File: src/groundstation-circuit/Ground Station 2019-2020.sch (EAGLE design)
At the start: 9 parts, among them U1 ADAFRUIT_RFM95W_LORA_RADIO

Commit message: Schematic and first routing attempt completed.
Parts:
- removed D1, D2, D3: (no value), SparkFun-LED:LED5MM
- added LED1, LED2, LED3: (no value), SparkFun-LED:LED5MM
- added R4: 220, SparkFun-Resistors:330OHM-HORIZ-1/10W-5%
- added R5: 1000, SparkFun-Resistors:330OHM-HORIZ-1/10W-5%
- renumbered J1 to HC-05
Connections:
- new net 3.3V: HC-05.2, U$1.3.3V, U1.VIN
- new net CS: U$1.10/TX2/PWM, U1.CS
- new net G0: U$1.8/TX3, U1.G0
- new net LED1: R3.2, U$1.2
- new net LED2: R2.2, U$1.3/CAN-TX/PWM
- new net LED3: R1.2, U$1.4/CAN-RX-PWM
- new net MISO: U$1.12/MISO, U1.MISO
- new net MOSI: U$1.11/MOSI, U1.MOSI
- new net N$1: LED3.A, R1.1
- new net N$3: LED1.A, R3.1
- new net N$4: R4.2, U$1.1/TX1/T
- new net RST: U$1.9/RX2/PWM, U1.RST
- new net RX1: HC-05.4, U$1.0/RX1/T
- new net SCK: U$1.13/SCK/LED, U1.SCK
- new net TX1: HC-05.5, R4.1, R5.2
- net GND: now also HC-05.3, LED1.C, LED2.C, LED3.C, R5.1
- net N$2: now also LED2.A, R2.1; no longer U1.VIN
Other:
- moved on the sheet: R1, R2, R3

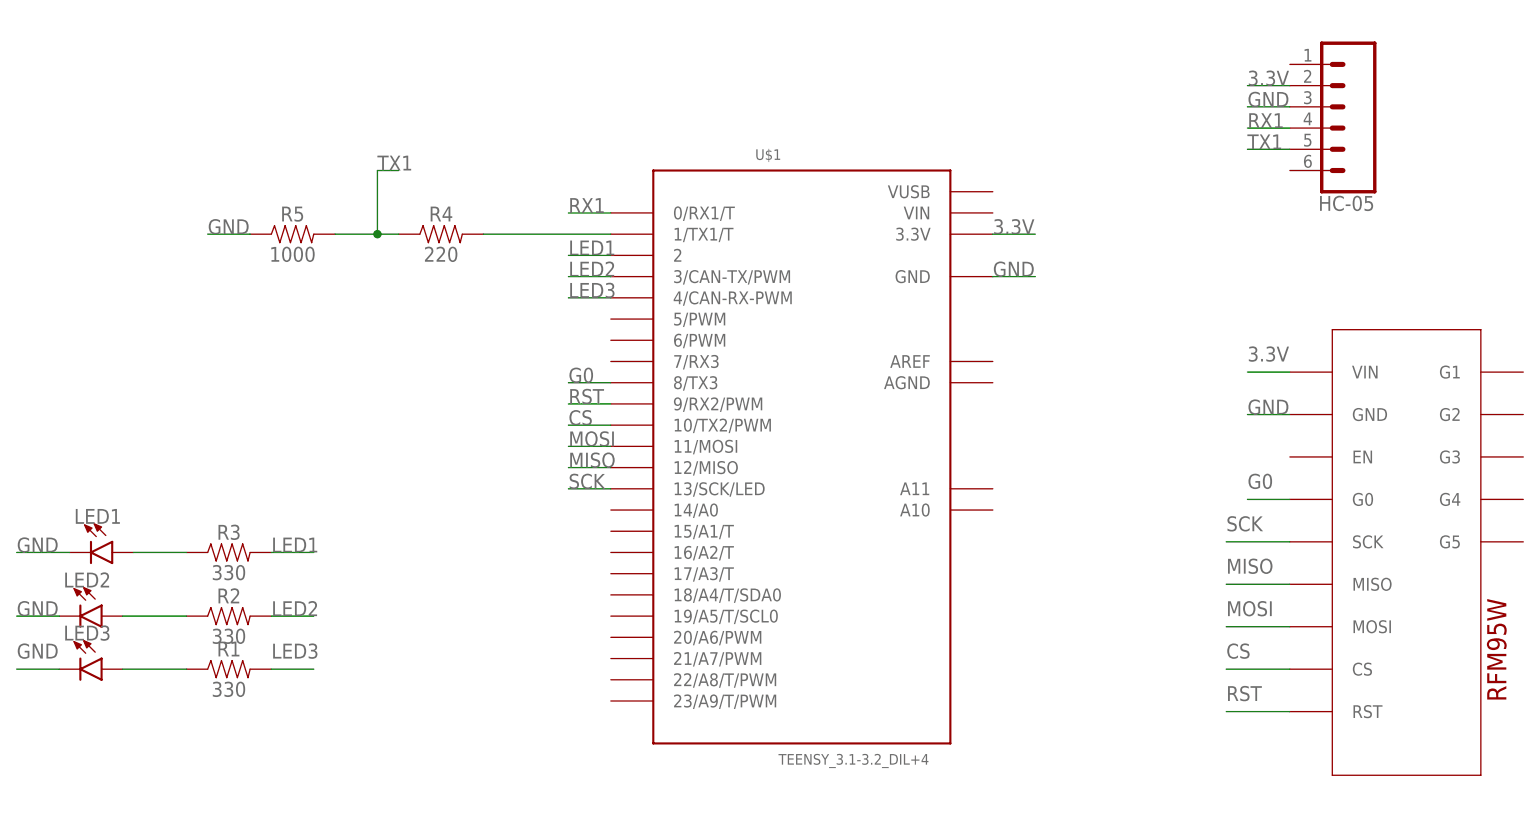
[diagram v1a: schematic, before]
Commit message: Added LCD to board and increased space to accomidate
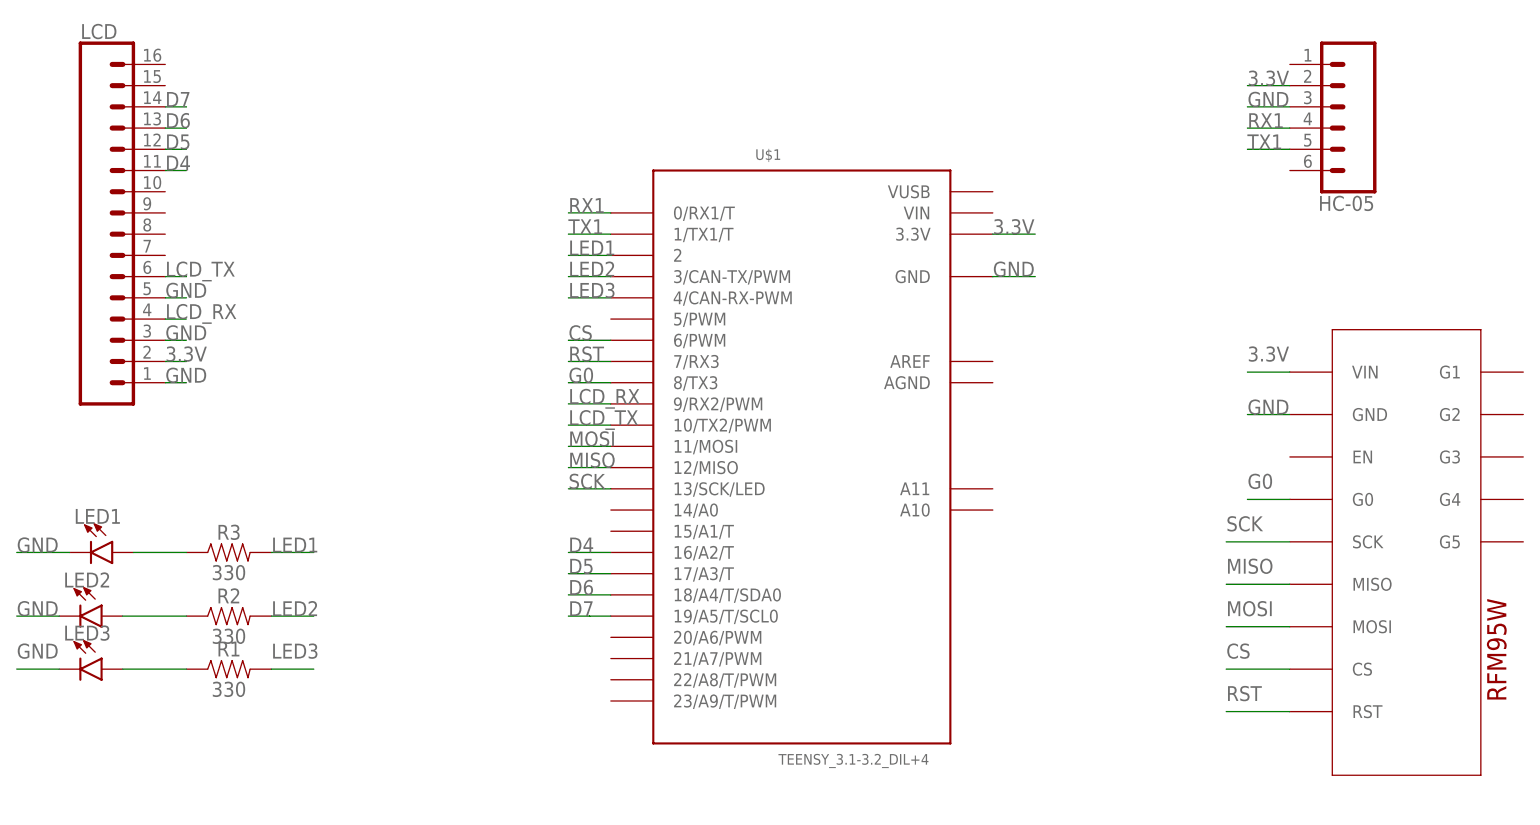
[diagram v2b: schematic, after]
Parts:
- removed R4: 220, SparkFun-Resistors:330OHM-HORIZ-1/10W-5%
- removed R5: 1000, SparkFun-Resistors:330OHM-HORIZ-1/10W-5%
- added LCD: (no value), SparkFun-Connectors:CONN_16
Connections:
- removed net N$4: R4.2, U$1.1/TX1/T
- new net D4: LCD.11, U$1.16/A2/T
- new net D5: LCD.12, U$1.17/A3/T
- new net D6: LCD.13, U$1.18/A4/T/SDA0
- new net D7: LCD.14, U$1.19/A5/T/SCL0
- new net LCD_RX: LCD.4, U$1.9/RX2/PWM
- new net LCD_TX: LCD.6, U$1.10/TX2/PWM
- net 3.3V: now also LCD.2
- net CS: now also U$1.6/PWM; no longer U$1.10/TX2/PWM
- net GND: now also LCD.1, LCD.3, LCD.5; no longer R5.1
- net RST: now also U$1.7/RX3; no longer U$1.9/RX2/PWM
- net TX1: now also U$1.1/TX1/T; no longer R4.1, R5.2

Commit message: Added additional LCD, mounting holes and slik screen.
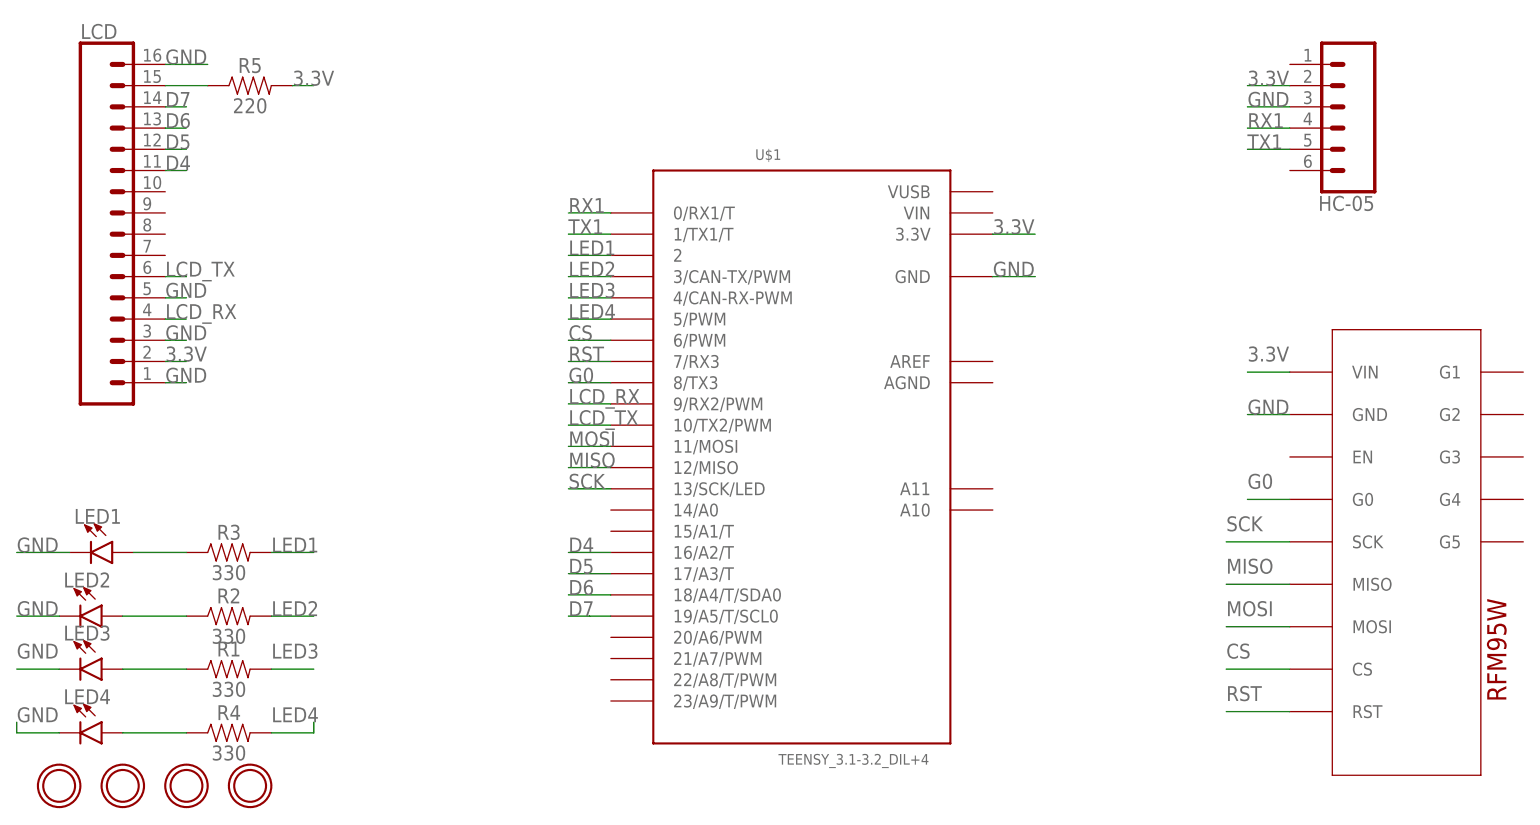
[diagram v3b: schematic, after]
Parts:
- added LED4: (no value), SparkFun-LED:LED5MM
- added R4: 330, SparkFun-Resistors:330OHM-HORIZ-1/10W-5%
- added R5: 220, SparkFun-Resistors:330OHM-HORIZ-1/10W-5%
- added U$2, U$3, U$4, U$5: MOUNTINGHOLE2.5, microbuilder:MOUNTINGHOLE2.5
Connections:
- new net LED4: R4.2, U$1.5/PWM
- new net N$4: LCD.15, R5.1
- new net N$5: LED4.A, R4.1
- net 3.3V: now also R5.2
- net GND: now also LCD.16, LED4.C
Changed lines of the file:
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@@
 <part name="R3" library="SparkFun-Resistors" library_urn="urn:adsk.eagle:library:532" deviceset="330OHM" device="-HORIZ-1/10W-5%" package3d_urn="urn:adsk.eagle:package:39658/1" value="330"/>
 <part name="LCD" library="SparkFun-Connectors" library_urn="urn:adsk.eagle:library:513" deviceset="CONN_16" device="" package3d_urn="urn:adsk.eagle:package:38258/1"/>
+<part name="U$2" library="microbuilder" deviceset="MOUNTINGHOLE" device="2.5"/>
+<part name="U$3" library="microbuilder" deviceset="MOUNTINGHOLE" device="2.5"/>
+<part name="U$4" library="microbuilder" deviceset="MOUNTINGHOLE" device="2.5"/>
+<part name="U$5" library="microbuilder" deviceset="MOUNTINGHOLE" device="2.5"/>
+<part name="R4" library="SparkFun-Resistors" library_urn="urn:adsk.eagle:library:532" deviceset="330OHM" device="-HORIZ-1/10W-5%" package3d_urn="urn:adsk.eagle:package:39658/1" value="330"/>
+<part name="LED4" library="SparkFun-LED" library_urn="urn:adsk.eagle:library:529" deviceset="LED" device="5MM" package3d_urn="urn:adsk.eagle:package:39353/1"/>
+<part name="R5" library="SparkFun-Resistors" library_urn="urn:adsk.eagle:library:532" deviceset="330OHM" device="-HORIZ-1/10W-5%" package3d_urn="urn:adsk.eagle:package:39658/1" value="220"/>
 </parts>
 <sheets>
@@
 <instance part="R3" gate="G$1" x="55.88" y="93.98"/>
 <instance part="LCD" gate="G$1" x="38.1" y="134.62"/>
+<instance part="U$2" gate="G$1" x="35.56" y="66.04"/>
+<instance part="U$3" gate="G$1" x="43.18" y="66.04"/>
+<instance part="U$4" gate="G$1" x="50.8" y="66.04"/>
+<instance part="U$5" gate="G$1" x="58.42" y="66.04"/>
+<instance part="R4" gate="G$1" x="55.88" y="72.39"/>
+<instance part="LED4" gate="G$1" x="40.64" y="72.39" rot="R270"/>
+<instance part="R5" gate="G$1" x="58.42" y="149.86"/>
 </instances>
 <busses>
@@
 <label x="48.26" y="124.46" size="1.778" layer="95"/>
 </segment>
+<segment>
+<pinref part="LED4" gate="G$1" pin="C"/>
+<wire x1="35.56" y1="72.39" x2="30.48" y2="72.39" width="0.1524" layer="91"/>
+<wire x1="30.48" y1="72.39" x2="30.48" y2="73.66" width="0.1524" layer="91"/>
+<label x="30.48" y="73.66" size="1.778" layer="95"/>
+</segment>
+<segment>
+<pinref part="LCD" gate="G$1" pin="16"/>
+<wire x1="48.26" y1="152.4" x2="53.34" y2="152.4" width="0.1524" layer="91"/>
+<label x="48.26" y="152.4" size="1.778" layer="95"/>
+</segment>
 </net>
 <net name="3.3V" class="0">
@@
 <wire x1="48.26" y1="116.84" x2="50.8" y2="116.84" width="0.1524" layer="91"/>
 <label x="48.26" y="116.84" size="1.778" layer="95"/>
+</segment>
+<segment>
+<pinref part="R5" gate="G$1" pin="2"/>
+<wire x1="63.5" y1="149.86" x2="66.04" y2="149.86" width="0.1524" layer="91"/>
+<label x="63.5" y="149.86" size="1.778" layer="95"/>
 </segment>
 </net>
@@
 </segment>
 </net>
+<net name="N$5" class="0">
+<segment>
+<pinref part="LED4" gate="G$1" pin="A"/>
+<pinref part="R4" gate="G$1" pin="1"/>
+<wire x1="43.18" y1="72.39" x2="50.8" y2="72.39" width="0.1524" layer="91"/>
+</segment>
+</net>
+<net name="LED4" class="0">
+<segment>
+<pinref part="U$1" gate="G$1" pin="5/PWM"/>
+<wire x1="101.6" y1="121.92" x2="96.52" y2="121.92" width="0.1524" layer="91"/>
+<label x="96.52" y="121.92" size="1.778" layer="95"/>
+</segment>
+<segment>
+<pinref part="R4" gate="G$1" pin="2"/>
+<wire x1="60.96" y1="72.39" x2="66.04" y2="72.39" width="0.1524" layer="91"/>
+<wire x1="66.04" y1="72.39" x2="66.04" y2="73.66" width="0.1524" layer="91"/>
+<label x="60.96" y="73.66" size="1.778" layer="95"/>
+</segment>
+</net>
+<net name="N$4" class="0">
+<segment>
+<pinref part="LCD" gate="G$1" pin="15"/>
+<pinref part="R5" gate="G$1" pin="1"/>
+<wire x1="48.26" y1="149.86" x2="53.34" y2="149.86" width="0.1524" layer="91"/>
+</segment>
+</net>
